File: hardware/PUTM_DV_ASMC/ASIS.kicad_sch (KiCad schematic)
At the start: 8 parts, among them Q4 BUK6D210, Q5 BUK6D210

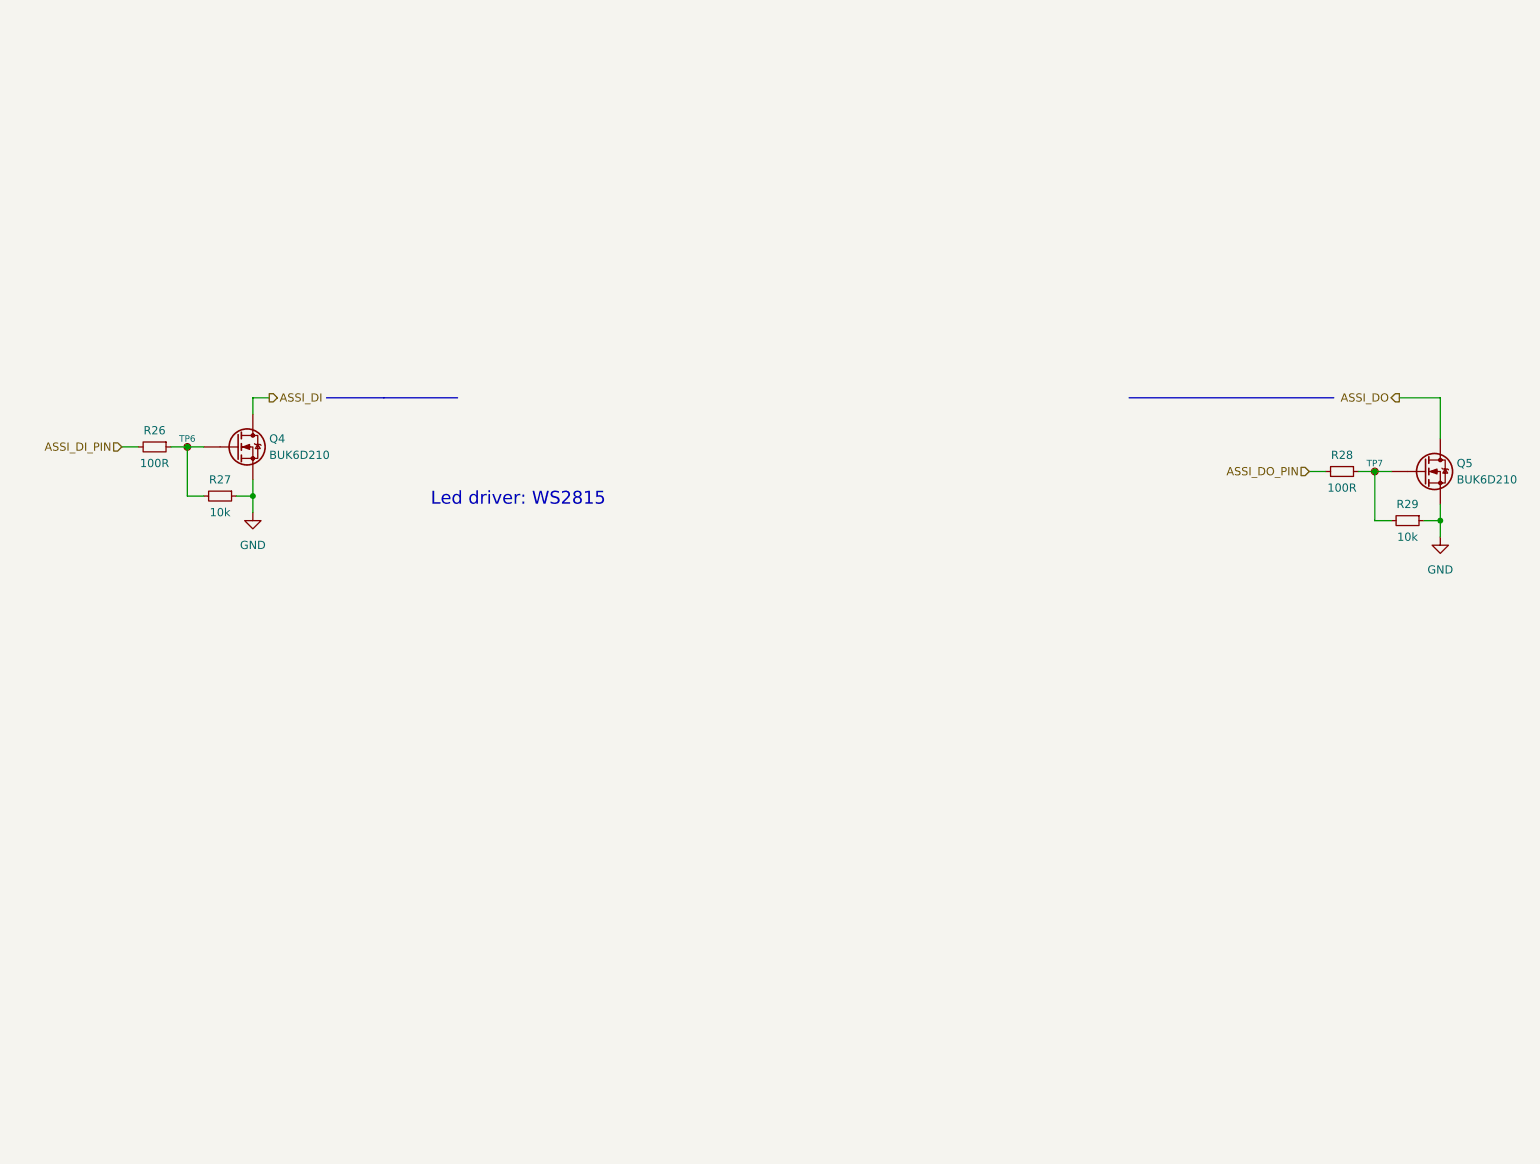
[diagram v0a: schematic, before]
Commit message: update assi logic on schema and update .ioc
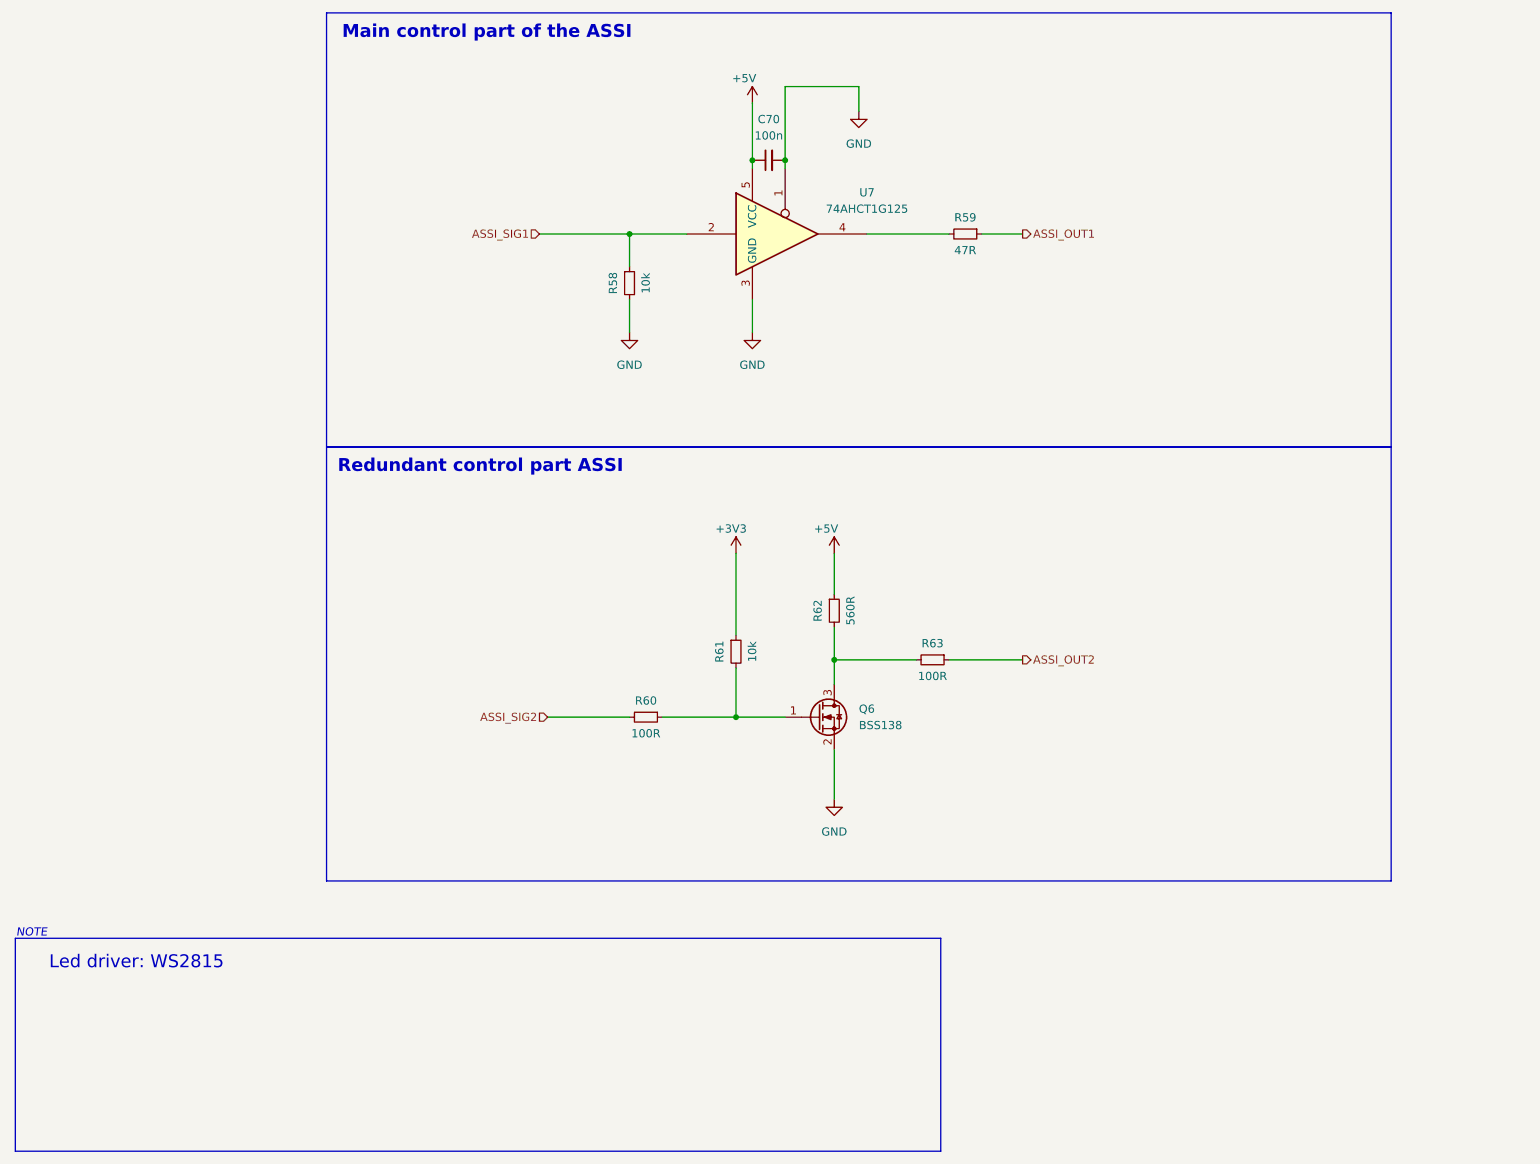
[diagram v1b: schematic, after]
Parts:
- removed Q4, Q5: BUK6D210, UDFN2020-6:Diodes_UDFN2020-6_Type-F, symbol BUK6D210:BUK6D210
- removed R26, R28: 100R, Resistor_SMD:R_0603_1608Metric, symbol Device:R_Small
- removed R27, R29: 10k, Resistor_SMD:R_0603_1608Metric, symbol Device:R_Small
- removed TP6, TP7: TestPoint_Small, TestPoint:TestPoint_Pad_D1.0mm, symbol Connector:TestPoint_Small
- added C70: 100n, Capacitor_SMD:C_0603_1608Metric_Pad1.08x0.95mm_HandSolder, symbol Device:C_Small
- added Q6: BSS138, Package_TO_SOT_SMD:SOT-23, symbol Transistor_FET:BSS138
- added R58, R61: 10k, Resistor_SMD:R_0603_1608Metric, symbol Device:R_Small
- added R59: 47R, Resistor_SMD:R_0603_1608Metric, symbol Device:R_Small
- added R60, R63: 100R, Resistor_SMD:R_0603_1608Metric, symbol Device:R_Small
- added R62: 560R, Resistor_SMD:R_0603_1608Metric, symbol Device:R_Small
- added U7: 74AHCT1G125, symbol 74xGxx:74AHCT1G125
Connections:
- net GND: now also C70.2, Q6.2 (S), R58.2, U7.1, U7.3 (GND)
- new net: Q6.3 (D), R62.2, R63.2
- new net: Q6.1 (G), R60.1, R61.2
- new net: R59.2, U7.4
- new net +3V3: R61.1
- new net +5V: C70.1, R62.1, U7.5 (VCC)
- new net ASSI_OUT1: R59.1
- new net ASSI_OUT2: R63.1
- new net ASSI_SIG1: R58.1, U7.2
- new net ASSI_SIG2: R60.2
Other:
- note added: "Main control part of the ASSI"
- note added: "NOTE"
- note added: "Redundant control part ASSI"

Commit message: update pcb layout
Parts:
- U7: footprint (none) -> Package_TO_SOT_SMD:SOT-23-5
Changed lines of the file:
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@@
 			)
 		)
-		(property "Footprint" ""
+		(property "Footprint" "Package_TO_SOT_SMD:SOT-23-5"
 			(at 143.51 52.07 0)
 			(hide yes)

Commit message: update pcb layout2
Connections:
- net +5V: now also C70.2; no longer C70.1
- net GND: now also C70.1; no longer C70.2
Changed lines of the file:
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@@
-	)
-	(junction
-		(at 138.43 40.64)
-		(diameter 0)
-		(color 0 0 0 0)
 	)
 	(junction
@@
 	)
 	(junction
-		(at 143.51 40.64)
+		(at 135.89 127)
 		(diameter 0)
 		(color 0 0 0 0)
 	)
 	(junction
-		(at 135.89 127)
+		(at 138.43 36.83)
 		(diameter 0)
 		(color 0 0 0 0)
@@
 	(wire
 		(pts
-			(xy 124.46 127) (xy 135.89 127)
+			(xy 124.46 36.83) (xy 124.46 39.37)
 		)
 		(stroke
@@
 	(wire
 		(pts
-			(xy 106.68 127) (xy 119.38 127)
+			(xy 124.46 127) (xy 135.89 127)
 		)
 		(stroke
@@
 	(wire
 		(pts
-			(xy 135.89 127) (xy 143.51 127)
+			(xy 133.35 36.83) (xy 138.43 36.83)
 		)
 		(stroke
@@
 	(wire
 		(pts
-			(xy 119.38 52.07) (xy 128.27 52.07)
+			(xy 106.68 127) (xy 119.38 127)
 		)
 		(stroke
@@
 	(wire
 		(pts
-			(xy 154.94 29.21) (xy 143.51 29.21)
+			(xy 135.89 127) (xy 143.51 127)
 		)
 		(stroke
@@
 	(wire
 		(pts
-			(xy 138.43 62.23) (xy 138.43 67.31)
+			(xy 119.38 52.07) (xy 128.27 52.07)
 		)
 		(stroke
@@
 	(wire
 		(pts
-			(xy 151.13 118.11) (xy 163.83 118.11)
+			(xy 154.94 29.21) (xy 143.51 29.21)
 		)
 		(stroke
@@
 	(wire
 		(pts
-			(xy 135.89 119.38) (xy 135.89 127)
+			(xy 138.43 62.23) (xy 138.43 67.31)
 		)
 		(stroke
@@
 	(wire
 		(pts
-			(xy 151.13 101.6) (xy 151.13 107.95)
+			(xy 151.13 118.11) (xy 163.83 118.11)
 		)
 		(stroke
@@
 	(wire
 		(pts
-			(xy 105.41 52.07) (xy 119.38 52.07)
+			(xy 135.89 119.38) (xy 135.89 127)
 		)
 		(stroke
@@
 	(wire
 		(pts
-			(xy 119.38 62.23) (xy 119.38 67.31)
+			(xy 151.13 101.6) (xy 151.13 107.95)
 		)
 		(stroke
@@
 	(wire
 		(pts
-			(xy 143.51 29.21) (xy 143.51 40.64)
+			(xy 105.41 52.07) (xy 119.38 52.07)
 		)
 		(stroke
@@
 	(wire
 		(pts
-			(xy 151.13 132.08) (xy 151.13 139.7)
+			(xy 119.38 62.23) (xy 119.38 67.31)
 		)
 		(stroke
@@
 	(wire
 		(pts
-			(xy 151.13 113.03) (xy 151.13 118.11)
+			(xy 143.51 29.21) (xy 143.51 41.91)
 		)
 		(stroke
@@
 	(wire
 		(pts
-			(xy 173.99 52.07) (xy 180.34 52.07)
+			(xy 151.13 132.08) (xy 151.13 139.7)
 		)
 		(stroke
@@
 	(wire
 		(pts
-			(xy 143.51 40.64) (xy 143.51 41.91)
+			(xy 151.13 113.03) (xy 151.13 118.11)
 		)
 		(stroke
@@
 	(wire
 		(pts
-			(xy 156.21 52.07) (xy 168.91 52.07)
+			(xy 173.99 52.07) (xy 180.34 52.07)
 		)
 		(stroke
@@
 	(wire
 		(pts
-			(xy 151.13 118.11) (xy 151.13 121.92)
+			(xy 128.27 36.83) (xy 124.46 36.83)
 		)
 		(stroke
@@
 	(wire
 		(pts
-			(xy 168.91 118.11) (xy 180.34 118.11)
+			(xy 156.21 52.07) (xy 168.91 52.07)
 		)
 		(stroke
@@
 	(wire
 		(pts
-			(xy 138.43 31.75) (xy 138.43 40.64)
+			(xy 151.13 118.11) (xy 151.13 121.92)
 		)
 		(stroke
@@
 	(wire
 		(pts
-			(xy 135.89 101.6) (xy 135.89 114.3)
+			(xy 168.91 118.11) (xy 180.34 118.11)
 		)
 		(stroke
@@
 	(wire
 		(pts
-			(xy 154.94 33.02) (xy 154.94 29.21)
+			(xy 135.89 101.6) (xy 135.89 114.3)
 		)
 		(stroke
@@
 	(wire
 		(pts
-			(xy 138.43 40.64) (xy 138.43 41.91)
+			(xy 154.94 33.02) (xy 154.94 29.21)
 		)
 		(stroke
@@
 	(wire
 		(pts
+			(xy 138.43 31.75) (xy 138.43 36.83)
+		)
+		(stroke
+			(width 0)
+			(type default)
+		)
+	)
+	(wire
+		(pts
 			(xy 119.38 52.07) (xy 119.38 57.15)
+		)
+		(stroke
+			(width 0)
+			(type default)
+		)
+	)
+	(wire
+		(pts
+			(xy 138.43 36.83) (xy 138.43 41.91)
 		)
 		(stroke
@@
 	)
 	(symbol
-		(lib_id "Device:C_Small")
-		(at 140.97 40.64 90)
-		(unit 1)
-		(body_style 1)
-		(exclude_from_sim no)
-		(in_bom yes)
-		(on_board yes)
-		(in_pos_files yes)
-		(dnp no)
-		(fields_autoplaced yes)
-		(property "Reference" "C70"
-			(at 140.9763 34.29 90)
-			(show_name no)
-			(do_not_autoplace no)
-			(effects
-				(font
-					(size 1.27 1.27)
-				)
-			)
-		)
-		(property "Value" "100n"
-			(at 140.9763 36.83 90)
-			(show_name no)
-			(do_not_autoplace no)
-			(effects
-				(font
-					(size 1.27 1.27)
-				)
-			)
-		)
-		(property "Footprint" "Capacitor_SMD:C_0603_1608Metric_Pad1.08x0.95mm_HandSolder"
-			(at 140.97 40.64 0)
-			(hide yes)
-			(show_name no)
-			(do_not_autoplace no)
-			(effects
-				(font
-					(size 1.27 1.27)
-				)
-			)
-		)
-		(property "Datasheet" ""
-			(at 140.97 40.64 0)
-			(hide yes)
-			(show_name no)
-			(do_not_autoplace no)
-			(effects
-				(font
-					(size 1.27 1.27)
-				)
-			)
-		)
-		(property "Description" "Unpolarized capacitor, small symbol"
-			(at 140.97 40.64 0)
-			(hide yes)
-			(show_name no)
-			(do_not_autoplace no)
-			(effects
-				(font
-					(size 1.27 1.27)
-				)
-			)
-		)
-		(property "Mouser Part Number" "."
-			(at 140.97 40.64 0)
-			(hide yes)
-			(show_name no)
-			(do_not_autoplace no)
-			(effects
-				(font
-					(size 1.27 1.27)
-				)
-			)
-		)
-		(pin "2"
-		)
-		(pin "1"
-		)
-		(instances
-			(project "PUTM_DV_ASMC"
-				(path "/b652b05a-4e3d-4ad1-b032-18886abe7d45/d075a50f-a25c-45f5-bd31-e195b1ffb400"
-					(reference "C70")
-					(unit 1)
-				)
-			)
-		)
-	)
-	(symbol
 		(lib_id "74xGxx:74AHCT1G125")
 		(at 143.51 52.07 0)
@@
 	)
 	(symbol
+		(lib_id "Device:C_Small")
+		(at 130.81 36.83 90)
+		(unit 1)
+		(body_style 1)
+		(exclude_from_sim no)
+		(in_bom yes)
+		(on_board yes)
+		(in_pos_files yes)
+		(dnp no)
+		(fields_autoplaced yes)
+		(property "Reference" "C70"
+			(at 130.8163 30.48 90)
+			(show_name no)
+			(do_not_autoplace no)
+			(effects
+				(font
+					(size 1.27 1.27)
+				)
+			)
+		)
+		(property "Value" "100n"
+			(at 130.8163 33.02 90)
+			(show_name no)
+			(do_not_autoplace no)
+			(effects
+				(font
+					(size 1.27 1.27)
+				)
+			)
+		)
+		(property "Footprint" "Capacitor_SMD:C_0603_1608Metric_Pad1.08x0.95mm_HandSolder"
+			(at 130.81 36.83 0)
+			(hide yes)
+			(show_name no)
+			(do_not_autoplace no)
+			(effects
+				(font
+					(size 1.27 1.27)
+				)
+			)
+		)
+		(property "Datasheet" ""
+			(at 130.81 36.83 0)
+			(hide yes)
+			(show_name no)
+			(do_not_autoplace no)
+			(effects
+				(font
+					(size 1.27 1.27)
+				)
+			)
+		)
+		(property "Description" "Unpolarized capacitor, small symbol"
+			(at 130.81 36.83 0)
+			(hide yes)
+			(show_name no)
+			(do_not_autoplace no)
+			(effects
+				(font
+					(size 1.27 1.27)
+				)
+			)
+		)
+		(property "Mouser Part Number" "."
+			(at 130.81 36.83 0)
+			(hide yes)
+			(show_name no)
+			(do_not_autoplace no)
+			(effects
+				(font
+					(size 1.27 1.27)
+				)
+			)
+		)
+		(pin "2"
+		)
+		(pin "1"
+		)
+		(instances
+			(project "PUTM_DV_ASMC"
+				(path "/b652b05a-4e3d-4ad1-b032-18886abe7d45/d075a50f-a25c-45f5-bd31-e195b1ffb400"
+					(reference "C70")
+					(unit 1)
+				)
+			)
+		)
+	)
+	(symbol
 		(lib_id "Device:R_Small")
 		(at 135.89 116.84 0)
@@
 					(unit 1)
 				)
+			)
+		)
+	)
+	(symbol
+		(lib_id "power:GND")
+		(at 124.46 39.37 0)
+		(unit 1)
+		(body_style 1)
+		(exclude_from_sim no)
+		(in_bom yes)
+		(on_board yes)
+		(in_pos_files yes)
+		(dnp no)
+		(property "Reference" "#PWR094"
+			(at 124.46 45.72 0)
+			(hide yes)
+			(show_name no)
+			(do_not_autoplace no)
+			(effects
+				(font
+					(size 1.27 1.27)
+				)
+			)
+		)
+		(property "Value" "GND"
+			(at 124.46 44.45 0)
+			(show_name no)
+			(do_not_autoplace no)
+			(effects
+				(font
+					(size 1.27 1.27)
+				)
+			)
+		)
+		(property "Footprint" ""
+			(at 124.46 39.37 0)
+			(hide yes)
+			(show_name no)
+			(do_not_autoplace no)
+			(effects
+				(font
+					(size 1.27 1.27)
+				)
+			)
+		)
+		(property "Datasheet" ""
+			(at 124.46 39.37 0)
+			(hide yes)
+			(show_name no)
+			(do_not_autoplace no)
+			(effects
+				(font
+					(size 1.27 1.27)
+				)
+			)
+		)
+		(property "Description" ""
+			(at 124.46 39.37 0)
+			(hide yes)
+			(show_name no)
+			(do_not_autoplace no)
+			(effects
+				(font
+					(size 1.27 1.27)
+				)
+			)
+		)
+		(pin "1"
+		)
+		(instances
+			(project "PUTM_DV_ASMC"
+				(path "/b652b05a-4e3d-4ad1-b032-18886abe7d45/d075a50f-a25c-45f5-bd31-e195b1ffb400"
+					(reference "#PWR094")
+					(unit 1)
+				)
